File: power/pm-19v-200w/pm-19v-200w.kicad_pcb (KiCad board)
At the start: 4 copper layers, 58.4 x 22.9 mm, 58 parts, among them J1 Brick 1/8 (DOSA), J2 Aux, Q1 BSC070N10NS5, Q2 BSC070N10NS5, Q3 BSC070N10NS5, Q4 BSC070N10NS5, U1 LTC7810, U2 MCP65R46-1.21, U3 MCP65R46-1.21

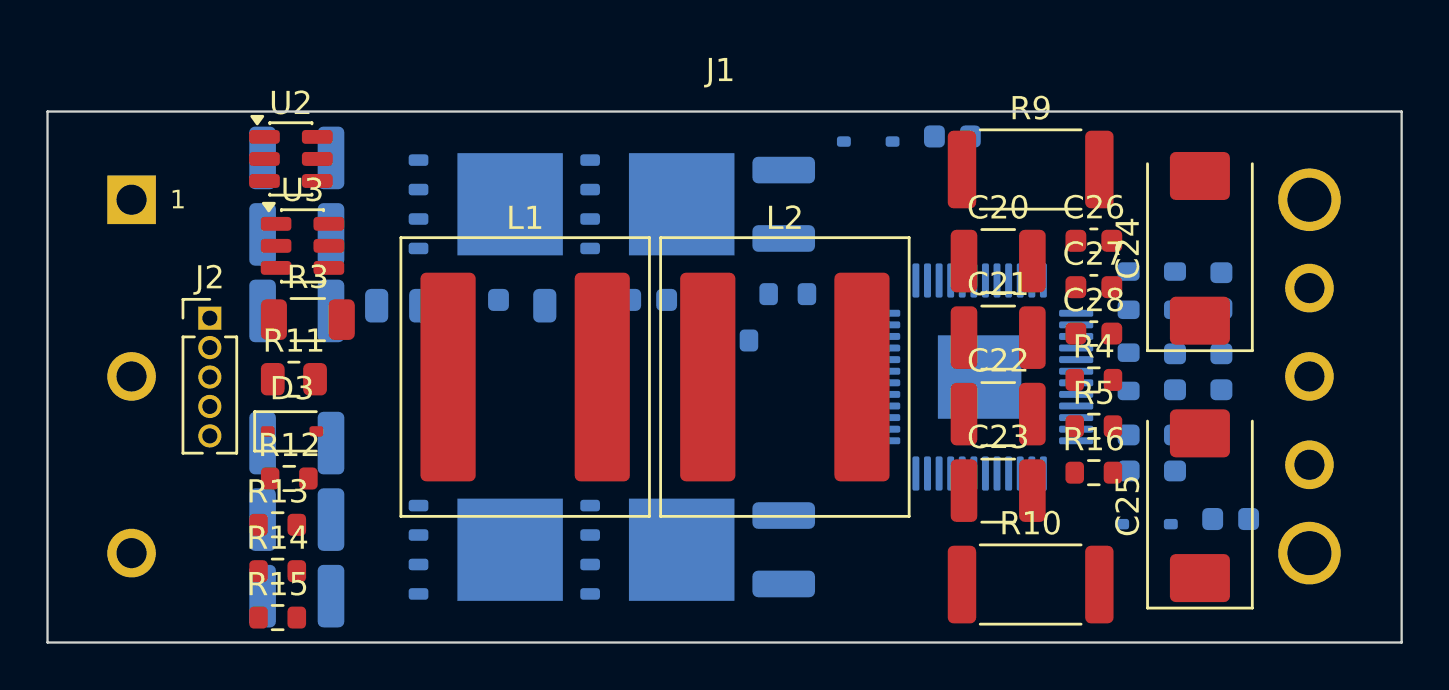
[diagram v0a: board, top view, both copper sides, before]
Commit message: pm-19v-200w: placement for routing, power pours and via fields, KRT first pass (12 opens left at U1)
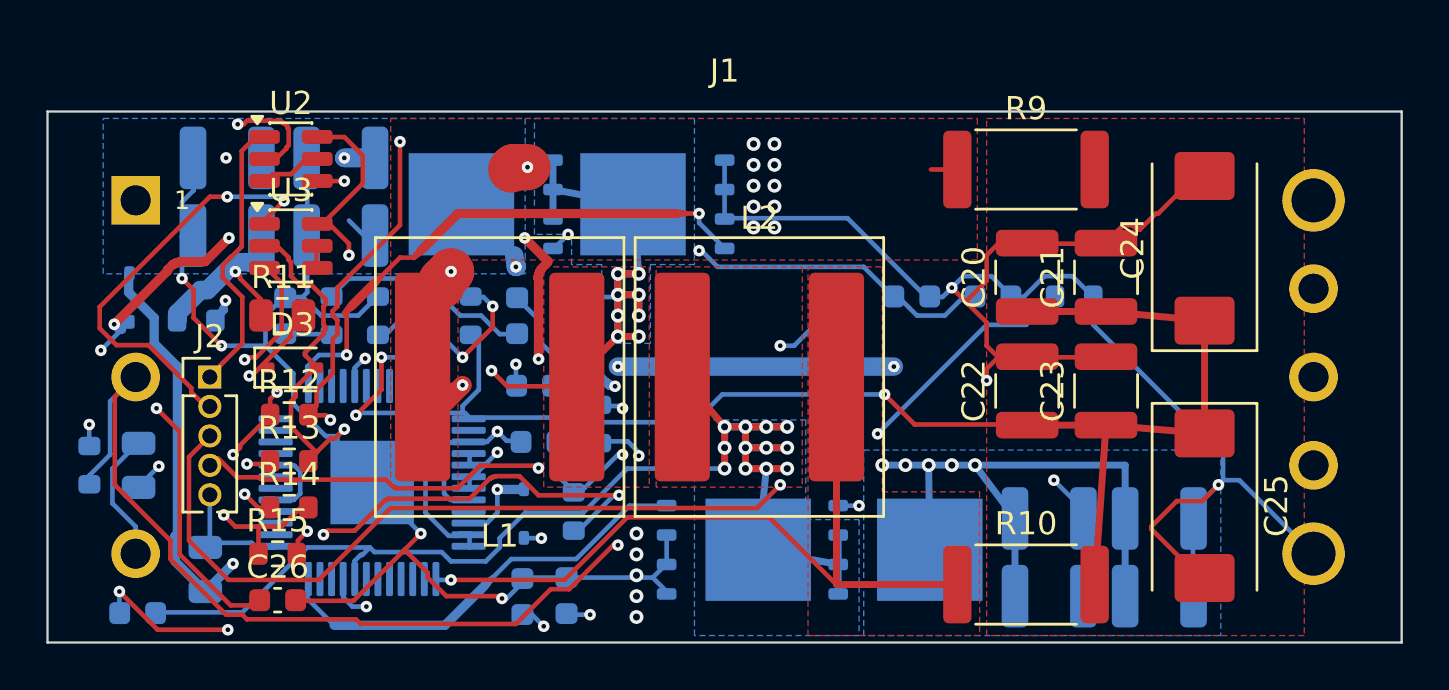
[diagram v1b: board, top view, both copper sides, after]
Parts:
- C27, C28, R16, R3, R4, R5: moved to B.Cu
- moved C19 47.3 mm to (103.9, 121.6)
- moved R4 43.5 mm to (101.8, 115.2), turned to 90 degrees
- moved C14 40.4 mm to (110.2, 108.8)
- moved C26 38.5 mm to (109.9, 121.1)
- moved C6 37.2 mm to (147.9, 117.5)
- moved R8 34.5 mm to (112.2, 108.8)
- moved C12 34.4 mm to (116.2, 108.8)
- moved R7 34.4 mm to (114.2, 108.8)
- moved C5 32.6 mm to (143.2, 117.5)
- moved D1 32.6 mm to (103.5, 108.0), turned to 90 degrees
- moved C7 32.4 mm to (143.2, 120.9)
- moved C13 28.5 mm to (120.2, 108.8)
- moved R6 28.4 mm to (118.2, 108.8)
- moved C17 27.0 mm to (122.4, 120.9)
- moved C16 26.9 mm to (120.5, 120.9)
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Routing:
- net GND: track 0.00 -> 215.0 mm, vias 0 -> 29
- net /VOUT: track 0.00 -> 85.3 mm, vias 0 -> 6
- net /VIN: track 0.00 -> 69.7 mm, vias 0 -> 11
- net /VAUX: track 0.00 -> 65.7 mm, vias 0 -> 4
- net /SW2: track 0.00 -> 61.7 mm, vias 0 -> 12
- net /RUN: track 0.00 -> 55.1 mm, vias 0 -> 2
- net /ID: track 0.00 -> 47.8 mm, vias 0 -> 2
- net /SW1: track 0.00 -> 37.9 mm, vias 0 -> 10
- net /BOOST1: track 0.00 -> 35.0 mm, vias 0 -> 6
- net /SNS2P: track 0.00 -> 33.8 mm, vias 0 -> 1
- net /DRVCC: track 0.00 -> 33.2 mm, vias 0 -> 2
- net /OVLO: track 0.00 -> 30.1 mm, vias 0 -> 3
- net /BOOST2: track 0.00 -> 23.9 mm, vias 0 -> 4
- net Net-(U2--): track 0.00 -> 23.7 mm, vias 0 -> 4
- net /BG1: track 0.00 -> 23.6 mm, vias 0 -> 2
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- added copper zone on F.Cu, net /SNS1P
- added copper zone on F.Cu, net /SNS2P
- added copper zone on B.Cu, net /SW1
- added copper zone on F.Cu, net /SW1
- added copper zone on B.Cu, net /SW2
- added copper zone on F.Cu, net /SW2
- added copper zone on B.Cu, net /VIN
- added copper zone on F.Cu, net /VOUT
- added copper zone on In2.Cu, net GND

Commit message: pm-19v-200w: supervisor off U1, Q4 GND vias back, reroute: 4 opens left
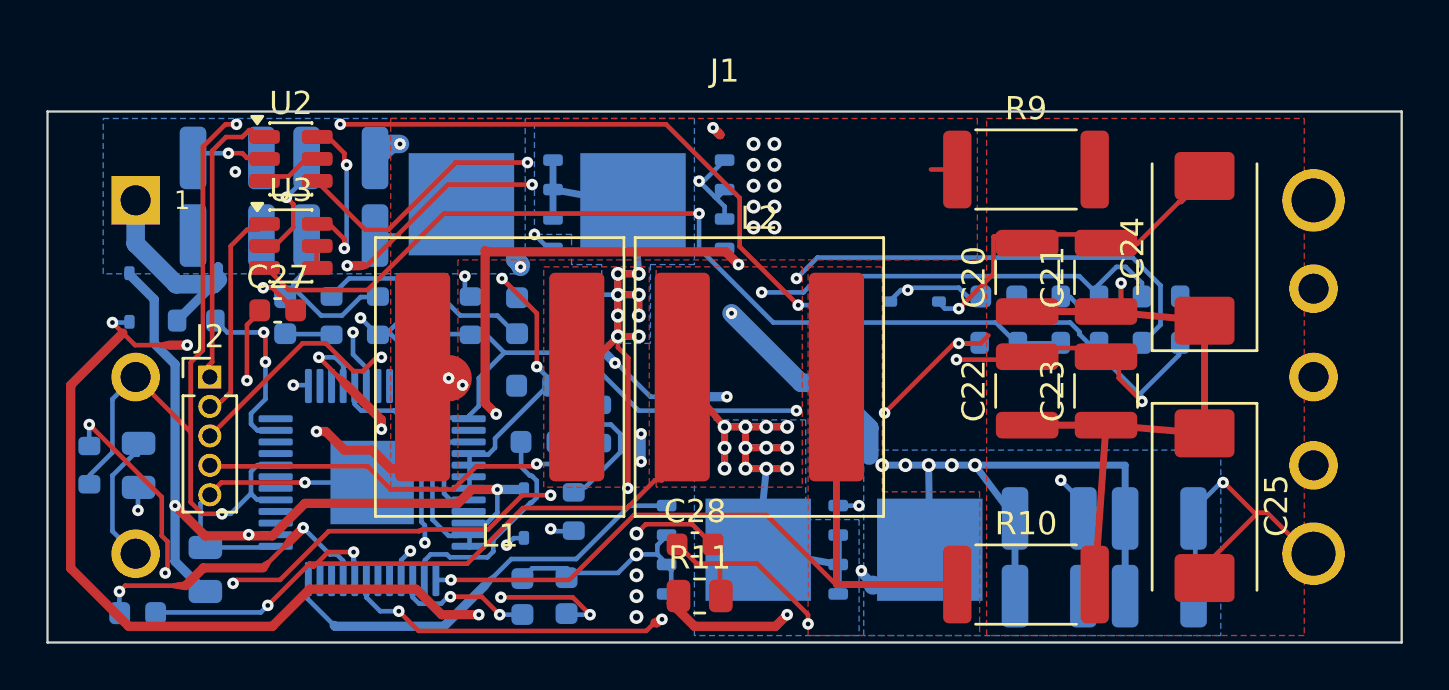
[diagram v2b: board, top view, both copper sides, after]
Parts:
- C26, D3, R12, R13, R14, R15: moved to B.Cu
- C27, C28: moved to F.Cu
- moved R13 38.3 mm to (148.0, 108.0)
- moved R15 35.8 mm to (144.5, 110.0)
- moved R12 34.5 mm to (144.5, 108.0)
- moved C26 33.7 mm to (141.0, 108.0)
- moved R14 31.4 mm to (141.0, 110.0)
- moved C27 27.4 mm to (109.9, 108.6)
- moved D3 27.0 mm to (137.4, 108.2)
- moved R11 21.7 mm to (128.1, 120.9)
- moved C28 16.7 mm to (127.9, 118.7)
- moved R16 4.25 mm to (148.0, 110.0)
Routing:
- net /BOOST1: track 35.0 -> 78.4 mm, vias 6 -> 9
- net GND: track 215.0 -> 189.4 mm, vias 29 -> 27
- net /TG2: track 0.91 -> 25.6 mm, vias 1 -> 3
- net /SNS1P: track 12.8 -> 37.4 mm, vias 3 -> 4
- net Net-(U2--): track 23.7 -> 42.3 mm, vias 4 -> 2
- net Net-(U3-+): track 21.9 -> 39.3 mm, vias 2 -> 1
- net /TG1: track 0.90 -> 17.8 mm, vias 1 -> 4
- net /SW1: track 37.9 -> 52.5 mm
- net Net-(U1-TRACK/SS2): track 1.05 -> 14.2 mm, vias 1 -> 3
- net /VAUX: track 65.7 -> 78.7 mm, vias 4 -> 5
- net /VOUT: track 85.3 -> 73.3 mm, vias 6 -> 4
- net /VIN: track 69.7 -> 80.7 mm
- net /PGOOD: track 17.9 -> 8.64 mm, vias 2 -> 0
- net /RUN: track 55.1 -> 62.5 mm, vias 2 -> 4
- net /INTVCC: track 6.96 -> 13.5 mm, vias 1 -> 0
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
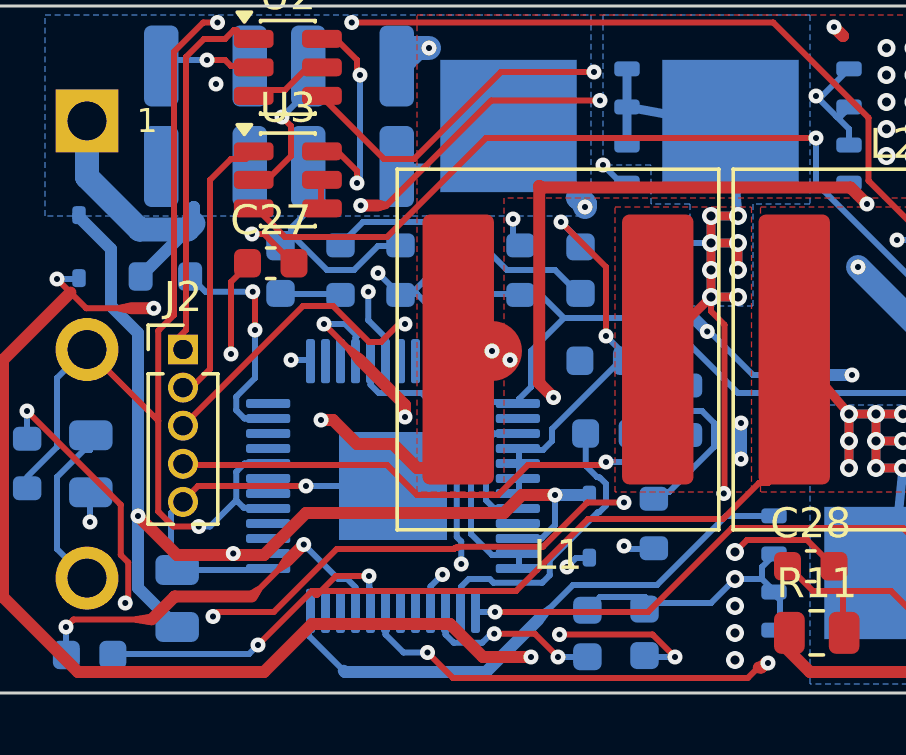
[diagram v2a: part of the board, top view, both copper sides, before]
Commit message: pm-19v-200w: hand-route the 4 U1 opens (OVLO, INTVCC, ITH1, TRACK/SS1); DRC 0 unconnected, 0 clearance
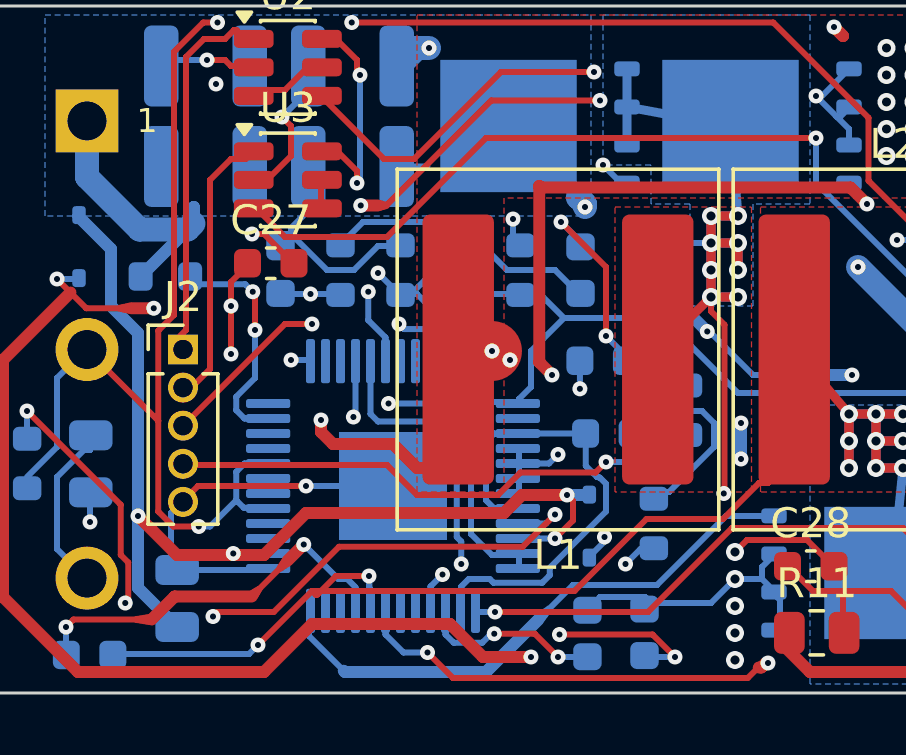
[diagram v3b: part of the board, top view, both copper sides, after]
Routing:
- net Net-(U1-TRACK/SS1): track 0.00 -> 10.3 mm, vias 0 -> 2
- net Net-(U1-ITH1): track 2.11 -> 8.16 mm, vias 0 -> 2
- net GND: track 189.4 -> 185.9 mm, vias 27 -> 28
- net /BOOST1: track 78.4 -> 75.8 mm, vias 9 -> 8
- net /INTVCC: track 13.5 -> 15.8 mm
- net /BOOST2: track 22.8 -> 24.4 mm
- net /OVLO: track 29.7 -> 30.9 mm
- net /VAUX: track 78.7 -> 78.0 mm, vias 5 -> 6
- net /DRVCC: track 35.0 -> 35.7 mm, vias 3 -> 4
- net /SW1: track 52.5 -> 53.0 mm
- net /BG1: track 29.0 -> 28.5 mm

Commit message: pm-19v-200w: gndpour after the U1 hand routing (F.Cu/B.Cu GND pours, 7 stitch vias); DRC 0 unconnected
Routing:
- net GND: vias 28 -> 35
- added copper zone on B.Cu, net GND
- added copper zone on F.Cu, net GND
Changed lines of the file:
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@@
 	)
 	(via
+		(at 156.95 102.95)
+		(size 0.6)
+		(drill 0.3)
+		(layers "F.Cu" "B.Cu")
+		(net "GND")
+	)
+	(via
 		(at 131.35 102.3)
 		(size 0.6)
@@
 	)
 	(via
+		(at 156.95 105.95)
+		(size 0.6)
+		(drill 0.3)
+		(layers "F.Cu" "B.Cu")
+		(net "GND")
+	)
+	(via
 		(at 131.35 105)
 		(size 0.6)
@@
 	)
 	(via
+		(at 156.95 117.95)
+		(size 0.6)
+		(drill 0.3)
+		(layers "F.Cu" "B.Cu")
+		(net "GND")
+	)
+	(via
 		(at 131.35 101.4)
 		(size 0.6)
@@
 	)
 	(via
+		(at 156.95 114.95)
+		(size 0.6)
+		(drill 0.3)
+		(layers "F.Cu" "B.Cu")
+		(net "GND")
+	)
+	(via
+		(at 156.95 120.95)
+		(size 0.6)
+		(drill 0.3)
+		(layers "F.Cu" "B.Cu")
+		(net "GND")
+	)
+	(via
+		(at 156.95 111.95)
+		(size 0.6)
+		(drill 0.3)
+		(layers "F.Cu" "B.Cu")
+		(net "GND")
+	)
+	(via
 		(at 128.1 103)
 		(size 0.5)
@@
 		(net "GND")
 	)
+	(via
+		(at 156.95 108.95)
+		(size 0.6)
+		(drill 0.3)
+		(layers "F.Cu" "B.Cu")
+		(net "GND")
+	)
 	(segment
 		(start 149.8 119.5)
@@
 	)
 	(zone
+		(net "GND")
+		(layer "F.Cu")
+		(hatch edge 0.5)
+		(priority 1)
+		(connect_pads
+			(clearance 0.25)
+		)
+		(min_thickness 0.25)
+		(fill yes
+			(thermal_gap 0.5)
+			(thermal_bridge_width 0.5)
+			(island_removal_mode 0)
+		)
+		(polygon
+			(pts
+				(xy 99.95 99.95) (xy 158.45 99.95) (xy 158.45 122.95) (xy 99.95 122.95)
+			)
+		)
+	)
+	(zone
 		(net "/VOUT")
 		(layer "F.Cu")
@@
 	)
 	(zone
+		(net "GND")
+		(layer "B.Cu")
+		(hatch edge 0.5)
+		(priority 1)
+		(connect_pads
+			(clearance 0.25)
+		)
+		(min_thickness 0.25)
+		(fill yes
+			(thermal_gap 0.5)
+			(thermal_bridge_width 0.5)
+			(island_removal_mode 0)
+		)
+		(polygon
+			(pts
+				(xy 99.95 99.95) (xy 158.45 99.95) (xy 158.45 122.95) (xy 99.95 122.95)
+			)
+		)
+	)
+	(zone
 		(net "/SW2")
 		(layer "B.Cu")
@@
 		)
 	)
+	(group "gnd-stitch"
+		(members "0b30837c-6604-4240-8d70-11b7d2614f89" "567d1673-0d2a-4339-aa3e-6a98d93ac6e0"
+			"8254afd4-e425-470d-9d12-e53b4cbf7cf7" "bad34837-f346-434e-8cc5-ed4ff21d3334"
+			"cbeec597-464b-446d-a2d9-11c99fa8d3b9" "d5678f73-3966-481c-8814-bc26da72a7c3"
+			"ff235519-6af3-48fd-8292-c141e6967de3"
+		)
+	)
